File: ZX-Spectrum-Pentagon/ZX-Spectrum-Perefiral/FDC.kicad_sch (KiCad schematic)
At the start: 64 parts

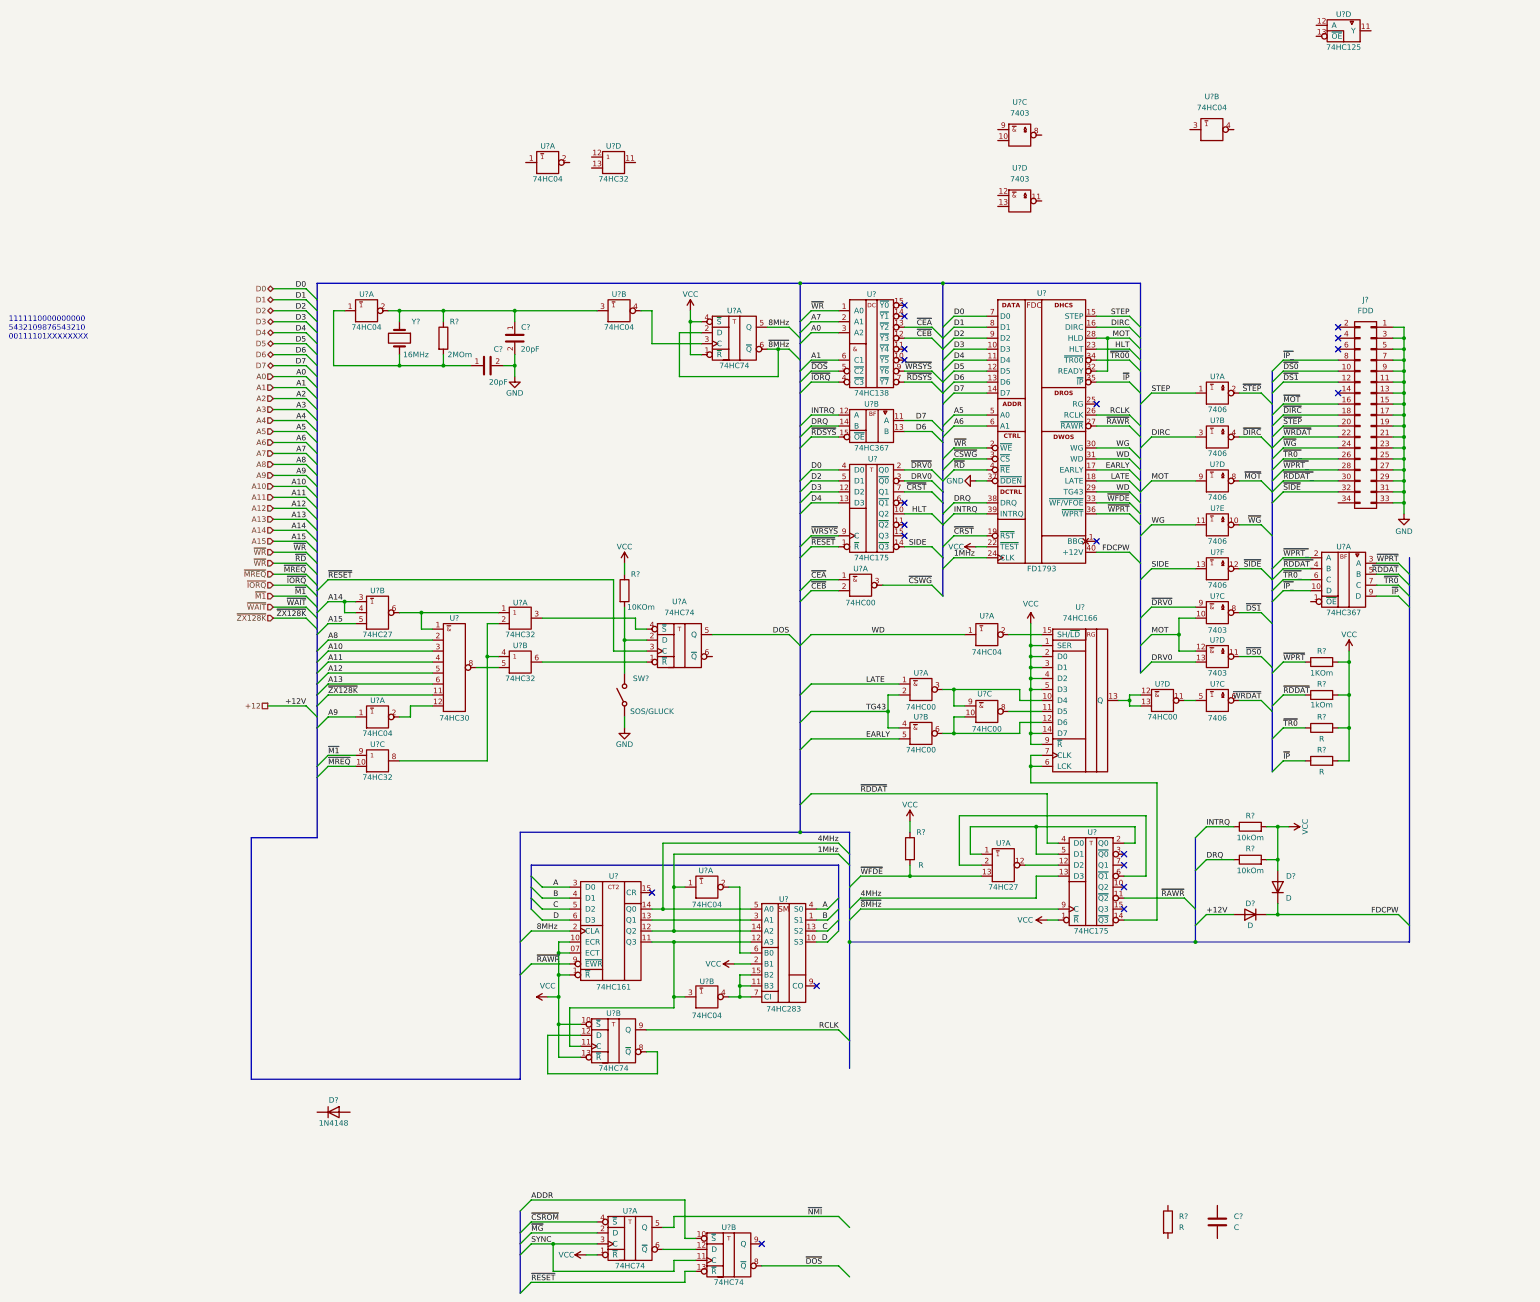
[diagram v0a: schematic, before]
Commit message: add keywords for some symbol in library 74IEC update some symbol in zx_custom_symbol improve FDC, Connectors, ZX-Spectrum-Perefiral schematic
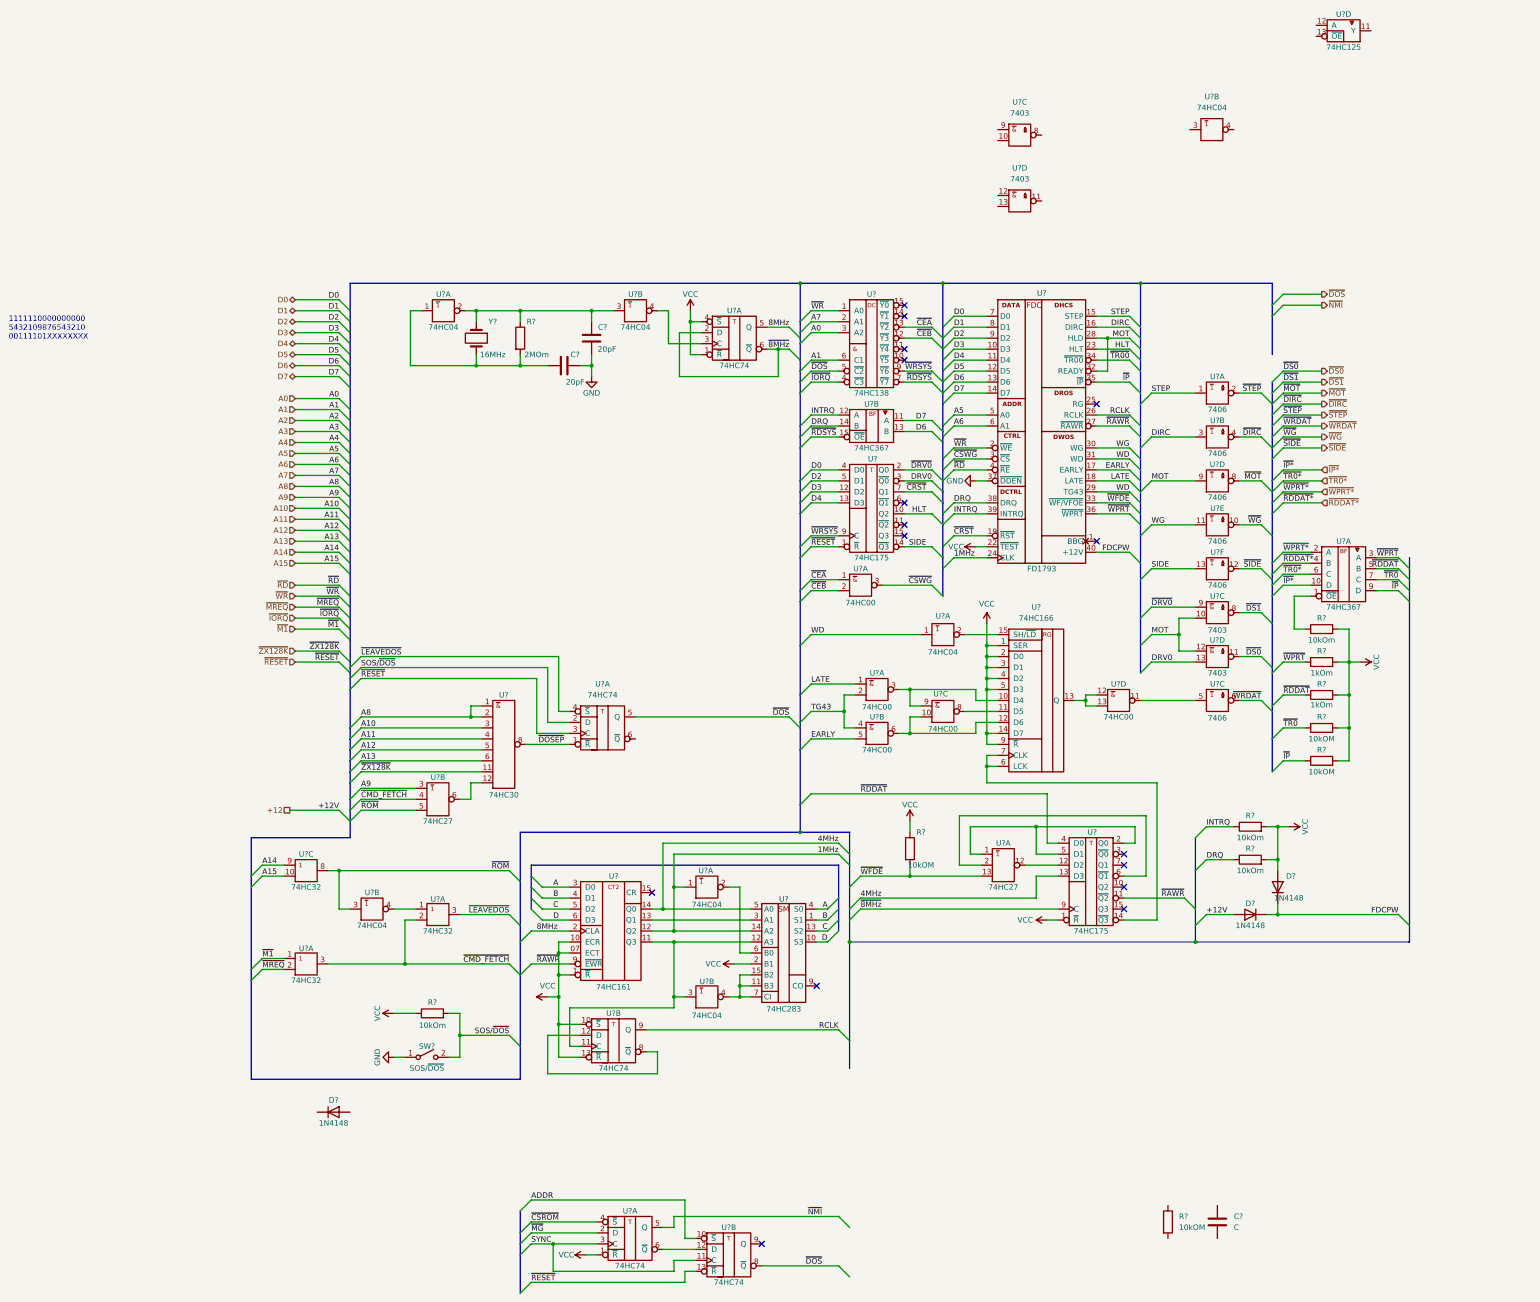
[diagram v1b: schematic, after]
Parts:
- removed C?: 20pF, Capacitor_SMD:C_0805_2012Metric_Pad1.18x1.45mm_HandSolder, symbol Device:C
- removed J?: FDD, symbol zx_custom_symbol:Conn_02x17_Odd_Even
- removed U? (x2): 74HC32, symbol 74IEC:74HC32
- removed U? (x2): 74HC04, Package_DIP:DIP-14_W7.62mm, symbol 74IEC:74HC04
- added C?: 20pF, Capacitor_SMD:C_0805_2012Metric_Pad1.18x1.45mm_HandSolder, symbol Device:C
- added R?: 10kOm, Resistor_SMD:R_0805_2012Metric, symbol Device:R
- added U?: 74HC32, symbol 74IEC:74HC32
- added U?: 74HC04, Package_DIP:DIP-14_W7.62mm, symbol 74IEC:74HC04
- D? (x2): value D -> 1N4148; footprint (none) -> Diode_SMD:D_MiniMELF
- D?: footprint Diode_SMD:D_MELF -> Diode_SMD:D_MiniMELF
- R? (x4): value R -> 10kOM
- R?: value 10KOm -> 10kOm
- R?: value 1KOm -> 1kOm
- SW?: value SOS/GLUCK -> SOS/~{DOS}
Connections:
- net DOS is gone; now on net ~{DOS}: U?.5 (Q)
- net A14: now also U?.9 (A); no longer U?.3 (A), U?.4 (B)
- net A15: now also U?.10 (B); no longer U?.5 (C)
- net A8: now also U?.1 (A)
- net A9: now also U?.3 (A)
- net GND: now also C?.2, U?.7 (GND), U?.7 (GND)
- net VCC: now also R?.2, U?.14 (VCC), U?.14 (VCC)
- net ~{M1}: now also U?.1 (A); no longer U?.9 (A)
- net ~{MREQ}: now also U?.2 (B); no longer U?.10 (B)
- net ~{WR}: no longer U?.4 (~{RE})
- net ~{CMD_FETCH}: now reaches U?.2 (B)
- net ~{CMD_FETCH}: now also U?.4 (B), U?.3 (Y); no longer U?.8 (Y)
- net ~{LEAVEDOS}: now reaches U?.3 (Y), U?.4 (~{S})
- net SOS/~{DOS}: now reaches R?.2, SW?.2 (B), U?.2 (D)
- net ~{DOSEP}: now reaches U?.1 (~{R})
- net ~{DOSEP}: now also U?.8 (~{Y})
- net at R?.2, U?.1 (A), Y?.2: now also C?.1
- net at U?.1 (~{OE}): now also R?.1
- net at U?.12 (H): now also U?.6 (~{Y})
- net ~{IP_} renamed ~{IP*}
- net ~{RDDAT_} renamed ~{RDDAT*}
- net ~{TR0_} renamed ~{TR0*}
- net ~{WPRT_} renamed ~{WPRT*}
- new net: U?.1 (A), U?.4 (~{Y})
- new net ~{RD}: U?.4 (~{RE})
- new net ~{ROM}: U?.3 (A), U?.5 (C), U?.8 (Y)
- no-connect marks 20 -> 16
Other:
- title: (none) -> ZX-Pentagon-Pereferal
- moved on the sheet: R?, U?, U?A, U?B, U?C, U?D, Y?

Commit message: improve schematic
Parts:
- removed C?: C, Capacitor_SMD:C_0805_2012Metric, symbol Device:C
- removed D?: 1N4148, Diode_SMD:D_MiniMELF, symbol Device:D
- removed R? (x2): 10kOM, Resistor_SMD:R_0805_2012Metric, symbol Device:R
- removed U? (x2): 7403, symbol 74IEC:7403
- removed U?: 74HC04, symbol 74IEC:74HC04
- removed U?: 74HC125, symbol 74IEC:74HC125
- added R?: 10kOM, Resistor_SMD:R_0805_2012Metric, symbol Device:R
- added U? (x2): 7403, Package_DIP:DIP-16_W7.62mm, symbol 74IEC:7403
- R? (x2): value 10kOM -> 1kOM
- U? (x14): footprint (none) -> Package_DIP:DIP-14_W7.62mm
- U? (x20): footprint (none) -> Package_DIP:DIP-16_W7.62mm
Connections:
- net 1MHz: now also U?.9 (A); no longer U?.1 (A)
- net A14: now also U?.1 (A); no longer U?.9 (A)
- net A15: now also U?.2 (B); no longer U?.10 (B)
- net DRV0: now also U?.5 (B); no longer U?.13 (B)
- net GND: now also U?.7 (GND), U?.7 (GND)
- net MOT: now also U?.2 (B), U?.4 (A); no longer U?.10 (B), U?.12 (A)
- net VCC: now also R?.2, U?.14 (VCC), U?.14 (VCC)
- net WD: now also U?.13 (A); no longer U?.1 (A)
- net ~{CMD_FETCH}: now also U?.10 (B), U?.6 (Y); no longer U?.2 (B), U?.3 (Y)
- net ~{DRV0}: now also U?.1 (A); no longer U?.9 (A)
- net ~{DS0}: now also U?.6 (~{Y}); no longer U?.11 (~{Y})
- net ~{DS1}: now also U?.3 (~{Y}); no longer U?.8 (~{Y})
- net ~{IP*}: now also R?.1
- net ~{IP}: no longer R?.1
- net ~{LEAVEDOS}: now also U?.8 (Y); no longer U?.3 (Y)
- net ~{M1}: now also U?.4 (A); no longer U?.1 (A)
- net ~{MREQ}: now also U?.5 (B); no longer U?.2 (B)
- net ~{RDDAT*}: now also R?.1
- net ~{RDDAT}: no longer R?.1
- net ~{ROM}: now also U?.3 (Y), U?.5 (A); no longer U?.3 (A), U?.8 (Y)
- net ~{TR0*}: now also R?.1
- net ~{TR0}: no longer R?.1
- net ~{WFDE}: now also R?.1
- net ~{WPRT*}: now also R?.1
- net ~{WPRT}: no longer R?.1
- net at U?.15 (SH/~{LD}): now also U?.12 (~{Y}); no longer U?.2 (~{Y})
- net at U?.11 (C), U?.11 (Q3), U?.12 (A3): now also U?.11 (A); no longer U?.3 (A)
- net at U?.6 (B0): now also U?.8 (~{Y}); no longer U?.2 (~{Y})
- net at U?.11 (B3), U?.15 (B2), U?.7 (CI): now also U?.10 (~{Y}); no longer U?.4 (~{Y})
- new net: U?.6 (~{Y}), U?.9 (A)
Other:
- moved on the sheet: D?, R?, U?A
